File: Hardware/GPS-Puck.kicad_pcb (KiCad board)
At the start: 2 copper layers, 44 x 44 mm, 17 parts, among them U1 Venus838LPx-L, U2 SKY65047-360LF

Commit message: Rough power layout
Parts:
- added B1: 3V, Batteries:Battery_ML-1220-F1AN, B.Cu at (164.5, 85.0)
- added C10: 1uF, Capacitors:CAPC1608N, B.Cu at (161.5, 99.5)
- added C11: 18pF, Capacitors:CAPC1608N, B.Cu at (141.5, 87.0)
- added C12: 10uF, Capacitors:CAPC2012N, B.Cu at (138.5, 84.5)
- added C9: 4.7uF, Capacitors:CAPC1608N, B.Cu at (138.5, 94.0)
- added D1: RB521, Diodes:SODFL1608N, B.Cu at (153.0, 85.5)
- added L3: 2.2uH, Inductors:INDC2012N, B.Cu at (138.5, 87.0)
- added R4: 390, Resistors:RESC1608N, B.Cu at (153.0, 87.5)
- added R5: 453k, Resistors:RESC1608N, B.Cu at (143.5, 87.0)
- added R6: 100k, Resistors:RESC1608N, B.Cu at (141.5, 90.5)
- added U3: NCP1521, SOT:SOT95P275-5L40N, B.Cu at (138.5, 90.5)

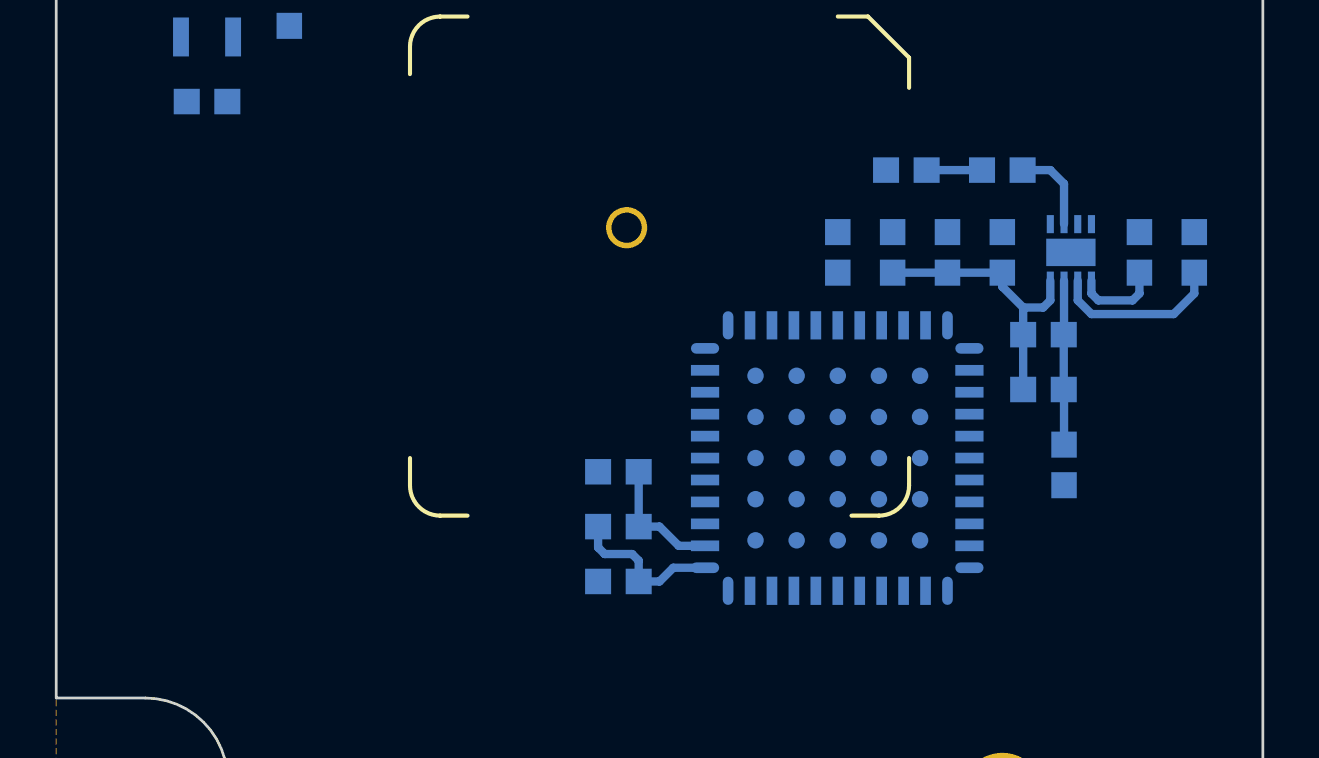
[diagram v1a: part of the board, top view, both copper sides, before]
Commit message: Add wire connector
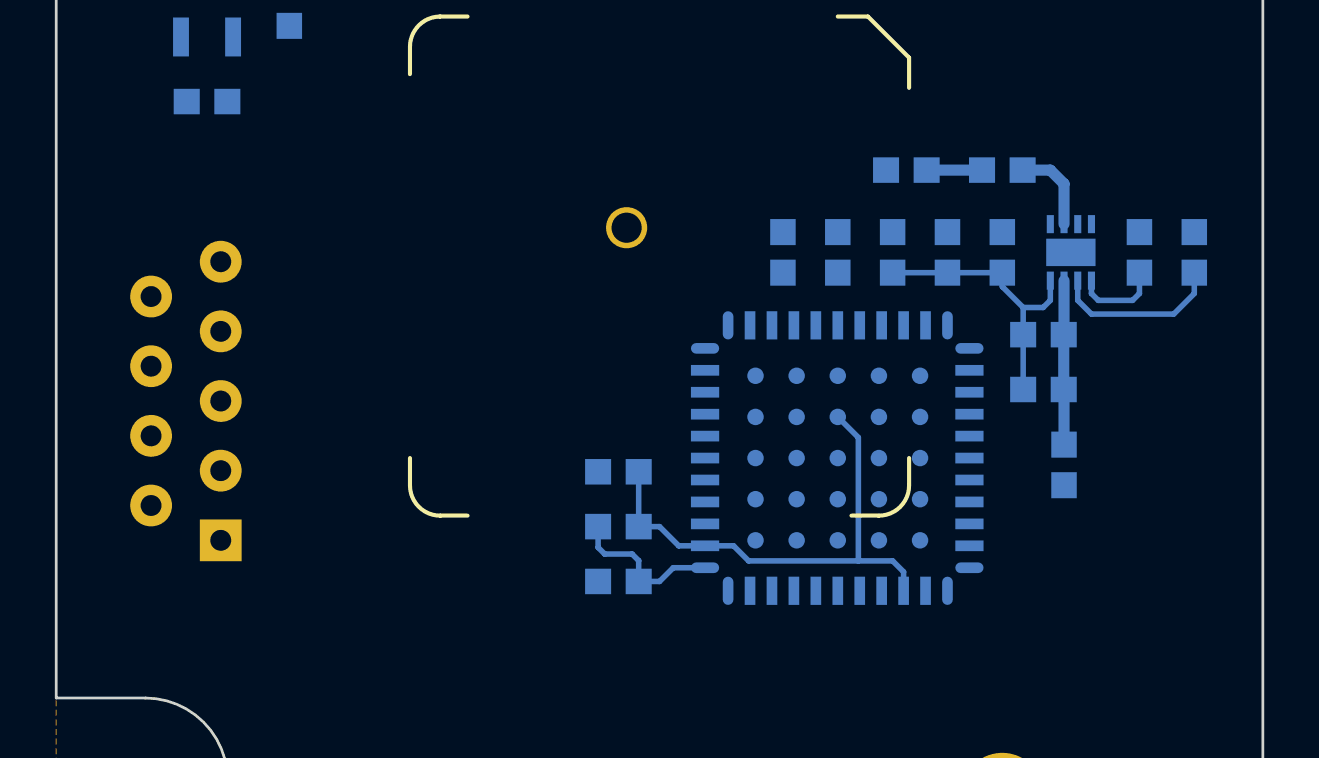
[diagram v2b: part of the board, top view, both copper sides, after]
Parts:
- added J1: Conn-9, Connectors:Conn_9-Wire-Pads, B.Cu at (139.0, 110.0)
- added R7: 0, Resistors:RESC1608N, B.Cu at (159.5, 99.5)
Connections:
- R4 pad 1: Net-(C10-Pad1) -> Net-(B1-Pad1)
- R4 pad 2: Net-(B1-Pad1) -> Net-(C10-Pad1)
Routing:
- net +3V3: track 18.3 -> 32.2 mm

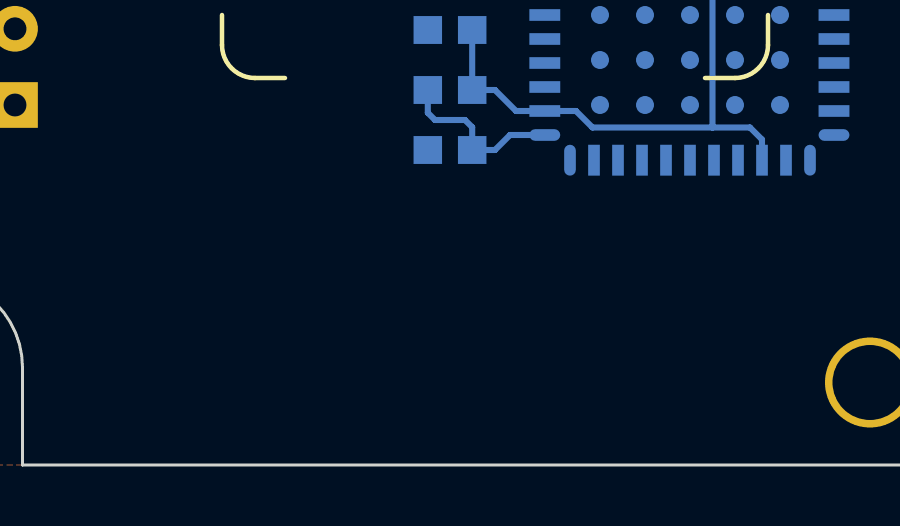
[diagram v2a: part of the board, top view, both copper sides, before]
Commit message: Add level translation
Closes #1
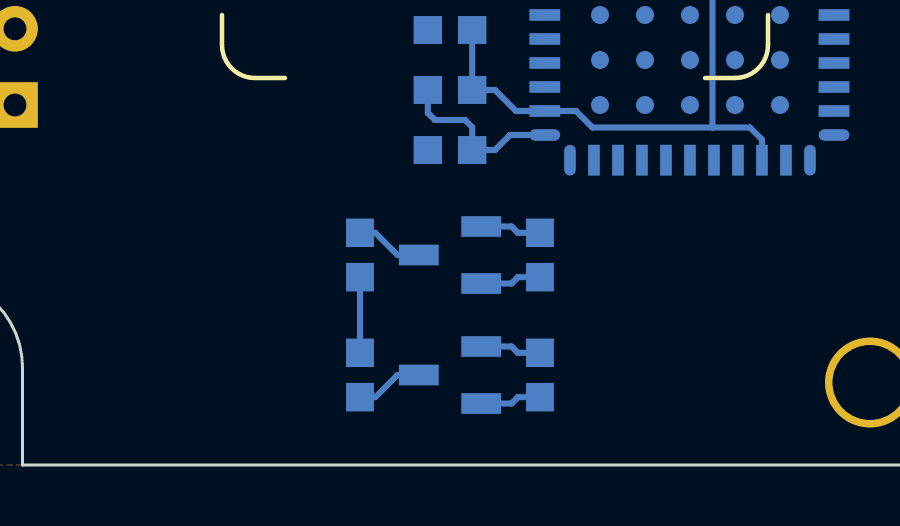
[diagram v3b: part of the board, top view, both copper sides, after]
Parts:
- added Q1: BSS138, SOT:SOT95P240-3N-GSD, B.Cu at (153.5, 115.0)
- added Q2: BSS138, SOT:SOT95P240-3N-GSD, B.Cu at (153.5, 119.0)
- added R10: 33k, Resistors:RESC1608N, B.Cu at (156.5, 119.0)
- added R11: 33k, Resistors:RESC1608N, B.Cu at (150.5, 119.0)
- added R8: 33k, Resistors:RESC1608N, B.Cu at (156.5, 115.0)
- added R9: 33k, Resistors:RESC1608N, B.Cu at (150.5, 115.0)
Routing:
- net +3V3: track 32.2 -> 36.3 mm
- net VCOM: track 0.00 -> 2.52 mm
- net /TxO: track 0.00 -> 2.27 mm
- net /RxI: track 0.00 -> 2.27 mm
- net /TX: track 0.00 -> 2.05 mm
- net /RX: track 0.00 -> 2.05 mm

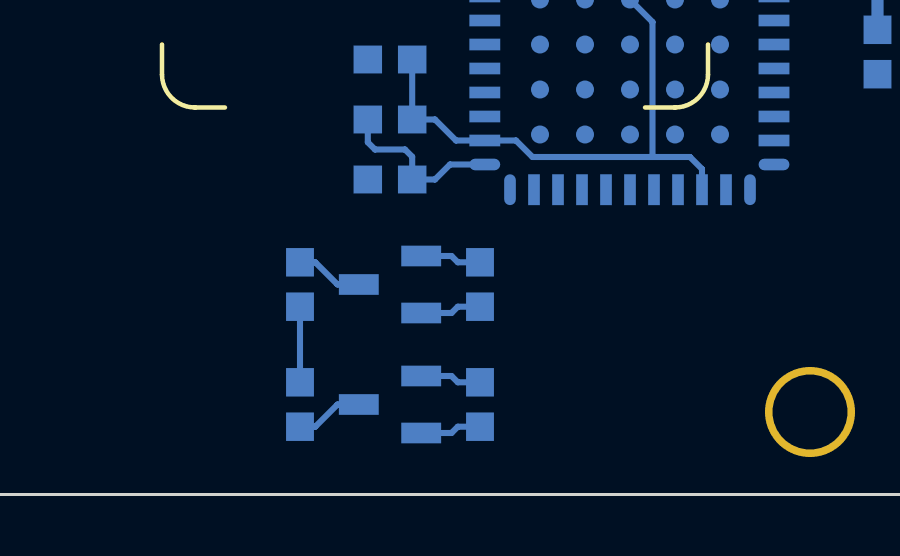
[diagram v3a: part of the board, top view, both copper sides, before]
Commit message: Add serial inverter
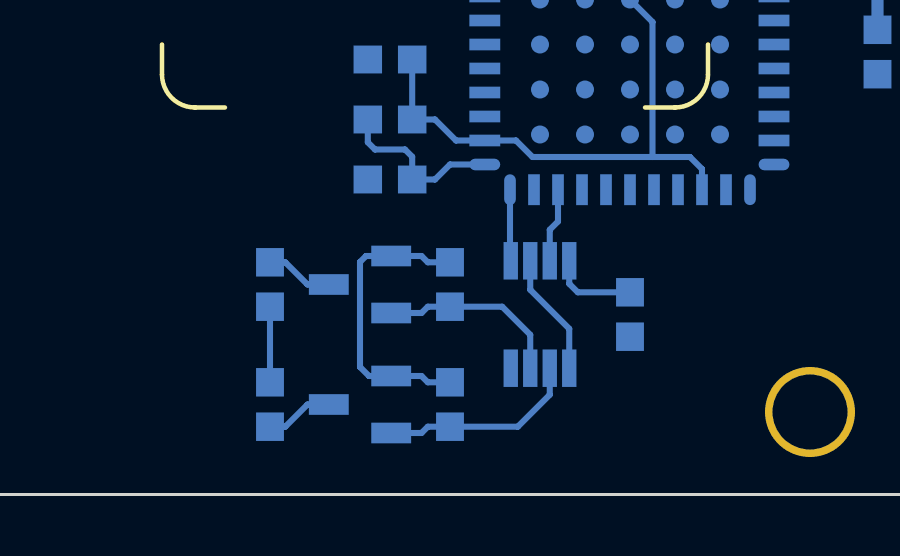
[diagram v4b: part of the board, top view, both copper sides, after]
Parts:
- added C13: 1uF, Capacitors:CAPC1608N, B.Cu at (161.5, 116.0)
- added U4: 74HC2G86, SOP:SOP65P400-8N, B.Cu at (158.5, 116.0)
- moved Q1 1.00 mm to (152.5, 115.0)
- moved Q2 1.00 mm to (152.5, 119.0)
- moved R10 1.00 mm to (155.5, 119.0)
- moved R11 1.00 mm to (149.5, 119.0)
- moved R8 1.00 mm to (155.5, 115.0)
- moved R9 1.00 mm to (149.5, 115.0)
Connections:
- Q1 pad S: /TX -> /TxL
- Q2 pad S: /RX -> /RxL
- R10 pad 2: /RX -> /RxL
- R8 pad 2: /TX -> /TxL
- U1 pad 42: /RX -> /Rx
- U1 pad 44: /TX -> /Tx
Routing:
- net +3V3: track 36.3 -> 45.0 mm
- net /RxL: track 0.00 -> 6.70 mm
- net /TxL: track 0.00 -> 6.22 mm
- net /Inv: track 0.00 -> 4.12 mm
- net /Rx: track 0.00 -> 2.48 mm
- net /Tx: track 0.00 -> 2.38 mm
- net /TX: track 2.05 -> 0.00 mm
- net /RX: track 2.05 -> 0.00 mm

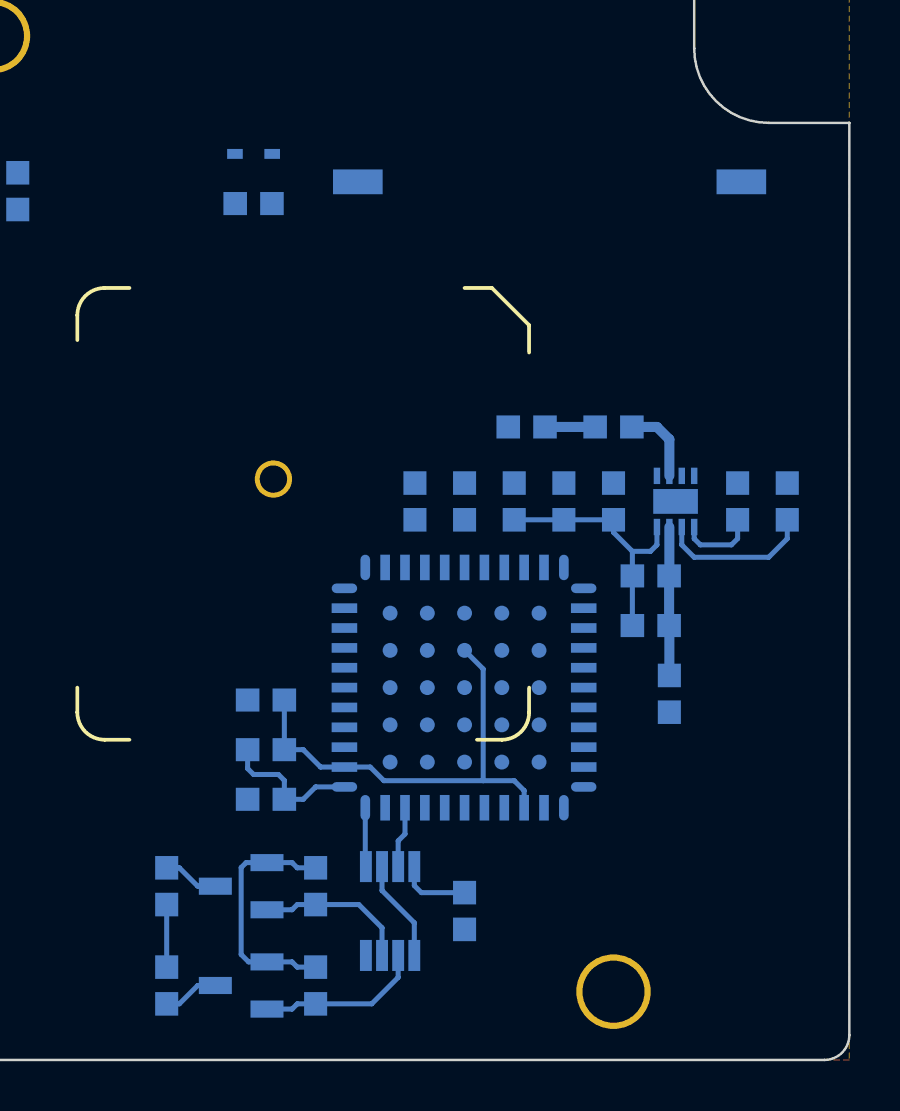
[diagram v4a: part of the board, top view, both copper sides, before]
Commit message: Add configuration jumpers
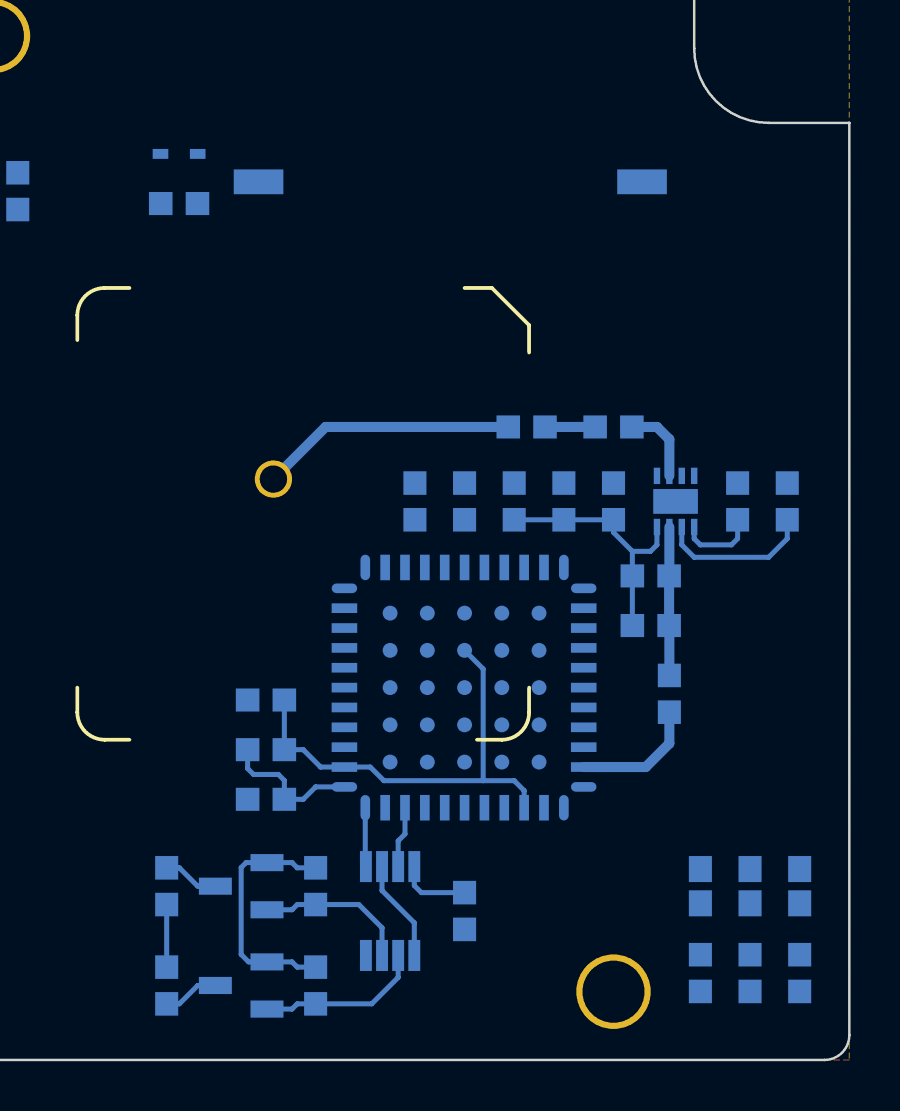
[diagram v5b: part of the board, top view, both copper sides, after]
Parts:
- added R12: 33k, Resistors:RESC1608N, B.Cu at (173.0, 118.5)
- added R13: 33k, Resistors:RESC1608N, B.Cu at (175.0, 118.5)
- added R14: 33k, Resistors:RESC1608N, B.Cu at (171.0, 118.5)
- added SB1: INV, Custom:SB1608N, B.Cu at (173.0, 115.0)
- added SB2: INV, Custom:SB1608N, B.Cu at (175.0, 115.0)
- added SB3: INV, Custom:SB1608N, B.Cu at (171.0, 115.0)
- moved B1 4.00 mm to (160.5, 85.0)
- moved D1 3.00 mm to (150.0, 85.5)
- moved R4 3.00 mm to (150.0, 87.5)
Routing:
- net /GPS0: track 0.00 -> 10.3 mm
- net /GPS4: track 0.00 -> 5.10 mm

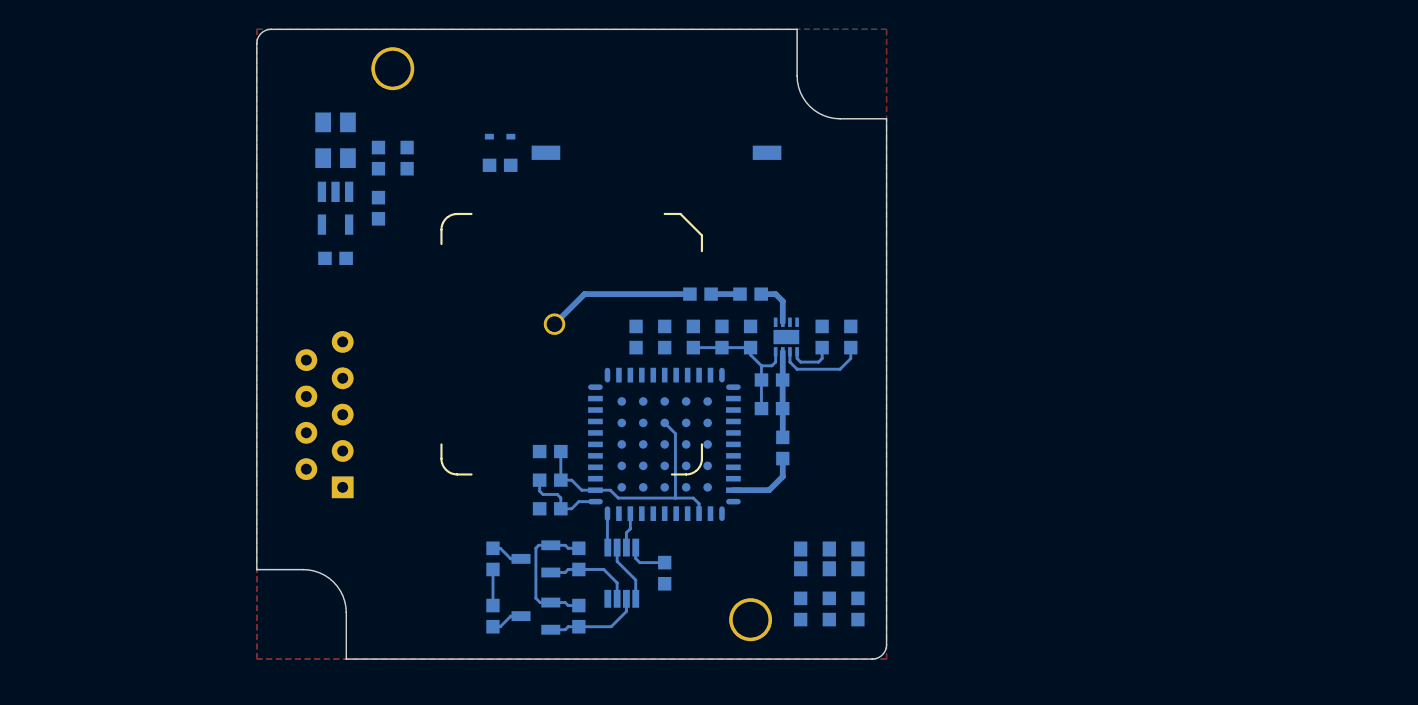
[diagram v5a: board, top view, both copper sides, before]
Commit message: Majority layout and routing
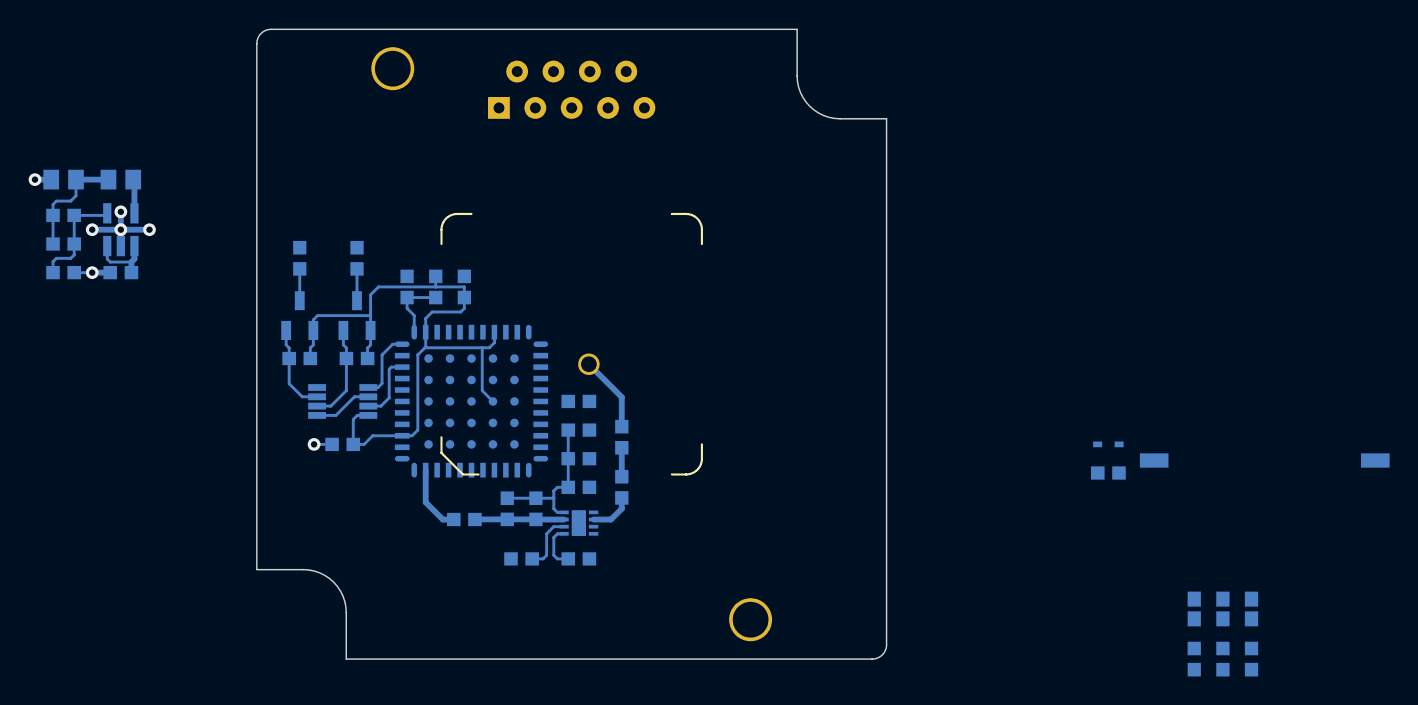
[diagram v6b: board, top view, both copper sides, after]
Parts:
- removed R7: 0, Resistors:RESC1608N
- moved B1 47.6 mm to (203.0, 106.5)
- moved D1 47.6 mm to (192.5, 107.0)
- moved R4 47.6 mm to (192.5, 109.0)
- moved J1 28.7 mm to (149.9, 83.5), turned to 0 degrees
- moved R3 27.7 mm to (151.5, 115.0), turned to 180 degrees
- moved R12 27.7 mm to (200.5, 122.0)
- moved R13 27.7 mm to (202.5, 122.0)
- moved R14 27.7 mm to (198.5, 122.0)
- moved SB1 27.7 mm to (200.5, 118.5)
- moved SB2 27.7 mm to (202.5, 118.5)
- moved SB3 27.7 mm to (198.5, 118.5)
- moved R11 26.7 mm to (140.0, 94.0)
- moved R9 25.0 mm to (136.0, 94.0), turned to 270 degrees
- moved Q2 24.4 mm to (140.0, 98.0), turned to 180 degrees
- moved R5 24.3 mm to (119.5, 91.0), turned to 0 degrees
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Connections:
- net Net-(L3-Pad1) renamed /Lx
- C3 pad 2: GNDA -> GND
- C5 pad 2: GNDA -> GND
- C6 pad 2: GNDA -> GND
- C7 pad 2: GNDA -> GND
- R3 pad 2: GNDA -> GND
- U1 pad 21: GNDA -> GND
- U1 pad 22: GNDA -> GND
- U1 pad 24: GNDA -> GND
- U1 pad 25: GNDA -> GND
- U1 pad 27: GNDA -> GND
- U1 pad 28: GNDA -> GND
- U1 pad 29: GNDA -> GND
- U1 pad 31: GNDA -> GND
- U1 pad 33: GNDA -> GND
- U1 pad 61: GNDA -> GND
- U1 pad 62: GNDA -> GND
- U1 pad 65: GNDA -> GND
- U1 pad 69: GNDA -> GND
- U2 pad 1: GNDA -> GND
- U2 pad 3: GNDA -> GND
- U2 pad 4: GNDA -> GND
- U2 pad 9: GNDA -> GND
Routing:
- net +3V3: track 45.0 -> 70.8 mm
- net GND: track 0.00 -> 11.3 mm, vias 0 -> 7
- net Net-(C11-Pad2): track 0.00 -> 7.57 mm
- net /GPS0: track 10.3 -> 5.31 mm
- net /Tx: track 2.38 -> 4.83 mm
- net /Lx: track 0.00 -> 2.39 mm
- net Net-(R3-Pad1): track 6.25 -> 4.04 mm
- net /Rx: track 2.48 -> 4.67 mm
- net VCOM: track 2.52 -> 4.62 mm
- net Net-(C2-Pad1): track 5.83 -> 4.63 mm
- removed copper zone on F.Cu, net GNDA
